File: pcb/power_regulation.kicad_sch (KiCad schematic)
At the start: 40 parts, among them U1 TPS563201, U3 TPS563201, U8 LM1085-5.0, U9 AMS1117-3.3

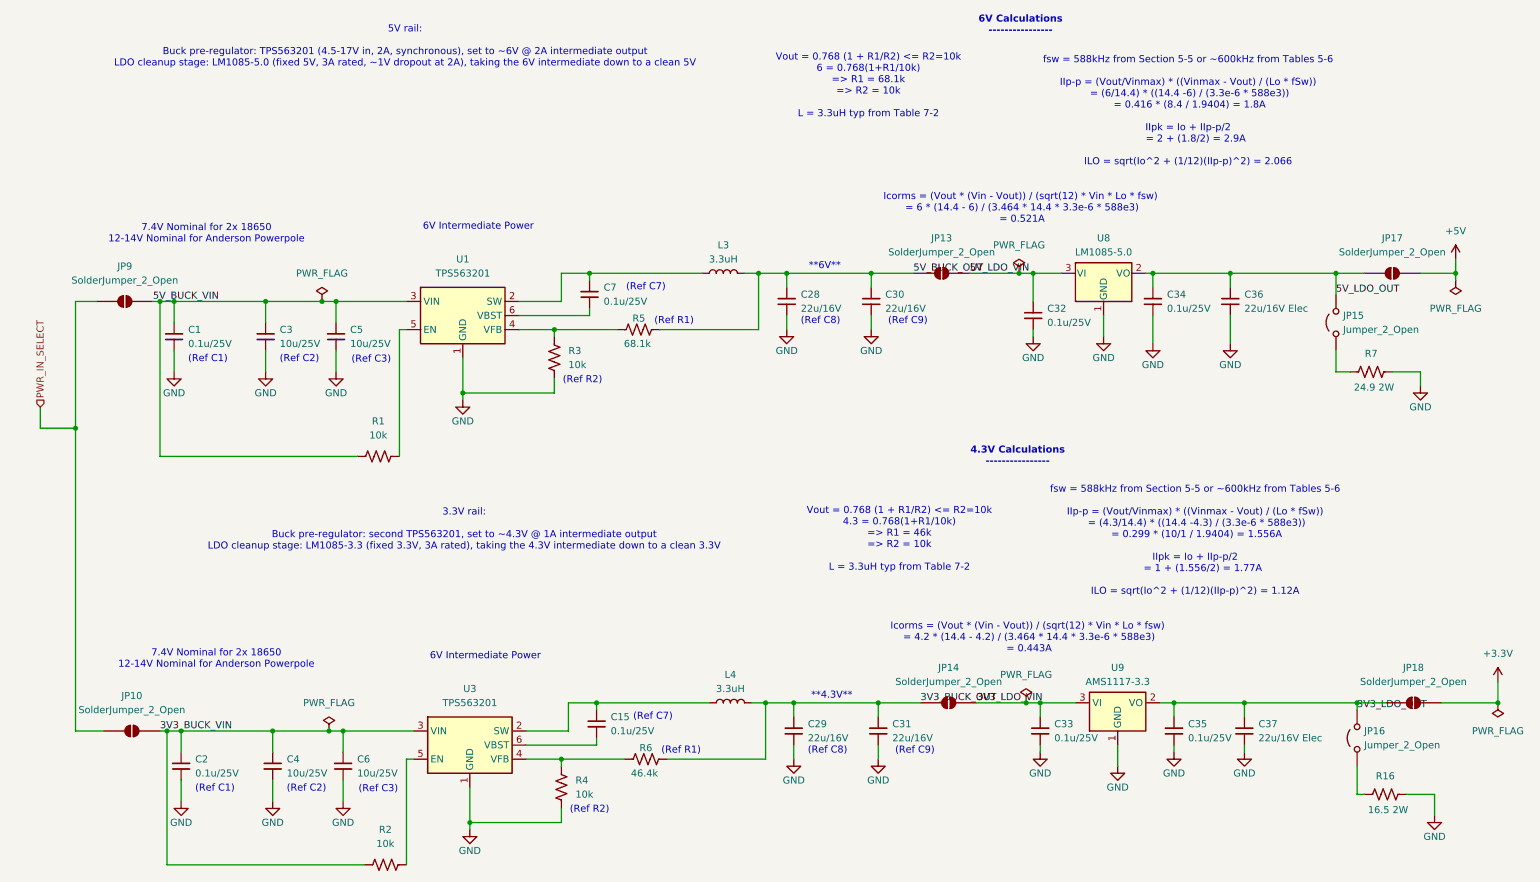
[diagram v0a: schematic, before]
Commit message: Add ESP32-S3 MCU sheet and CH340C USB-UART programming bridge
Restructures the schematic hierarchy: root sheet now hosts three
top-level sheets (Power, mcu-esp32, USB-C Programming UART) instead of
the old flat layout, with the battery/12V ORing-FET merge circuit
moved into its own dedicated Power sheet. Adds the ESP32-S3-WROOM-1
MCU sheet (native USB-C connector stubbed in but not yet wired) and a
CH340C-based USB-UART bridge with auto-reset/bootloader transistor
circuit for programming.

This is a work-in-progress checkpoint — several nets in the new sheets
(MCU decoupling, CH340C power, auto-reset routing, ORing FET gate
drive) still need wiring before ERC will be clean; see prior review
notes for the punch list.

Co-Authored-By: Claude Sonnet 5 <noreply@anthropic.com>
Claude-Session: https://claude.ai/code/session_01LwTJQ9pyVNMigbu4uLMh8c
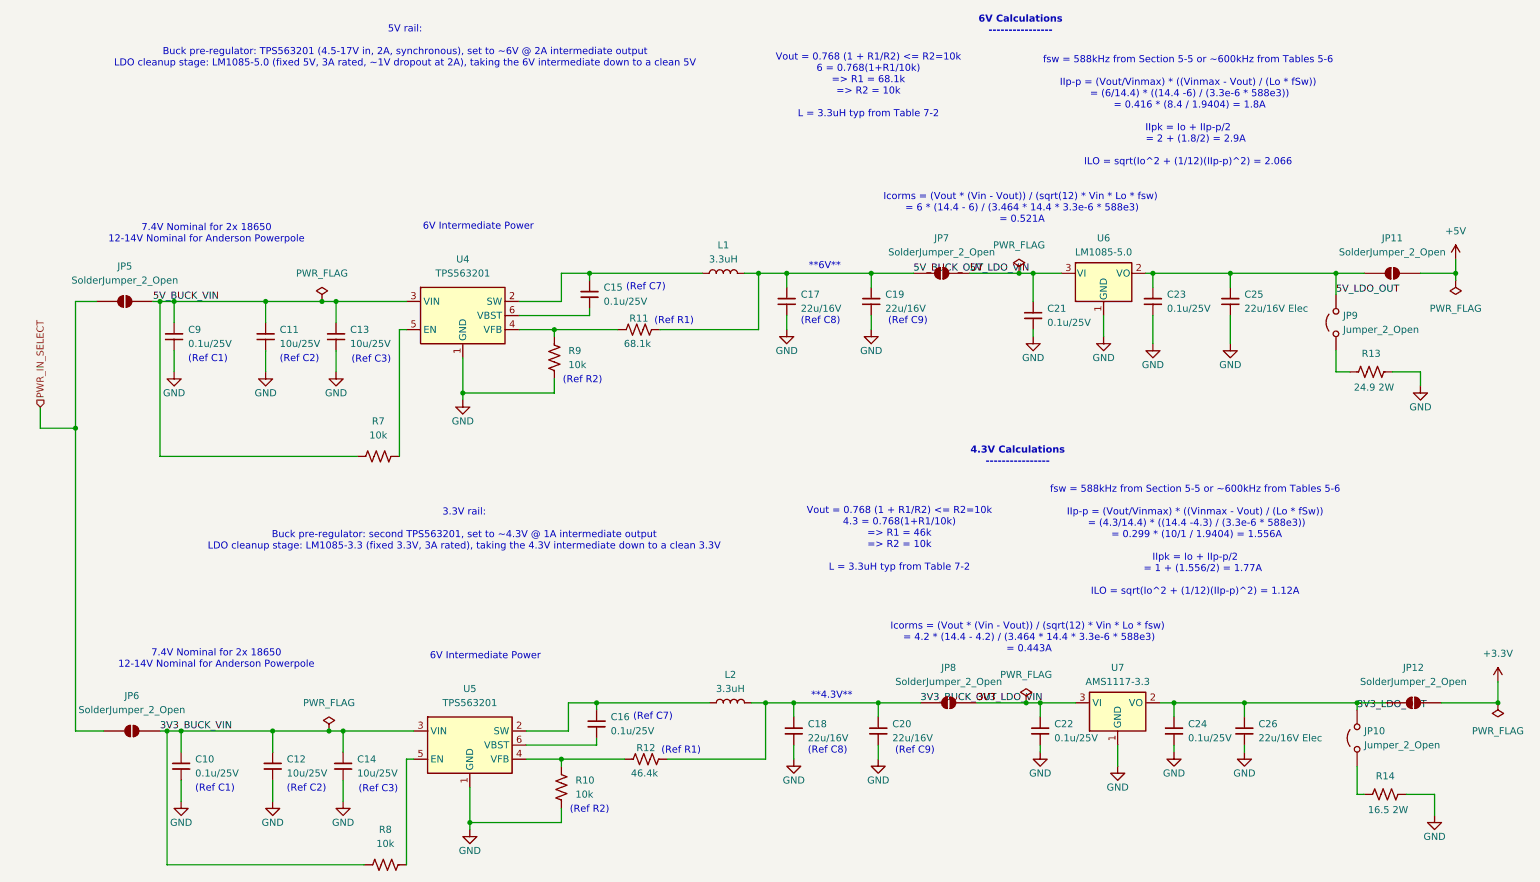
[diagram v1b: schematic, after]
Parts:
- renumbered C2 to C10, C3 to C11, C4 to C12, C5 to C13, C6 to C14, C7 to C15, C15 to C16, C28 to C17, C29 to C18, C30 to C19, C31 to C20, C32 to C21, C33 to C22, C34 to C23, C35 to C24, C36 to C25, C37 to C26, C1 to C9, JP16 to JP10, JP17 to JP11, JP18 to JP12, JP9 to JP5, JP10 to JP6, JP13 to JP7, JP14 to JP8, JP15 to JP9, L3 to L1, L4 to L2, R4 to R10, R5 to R11, R6 to R12, R7 to R13, R16 to R14, R1 to R7, R2 to R8, R3 to R9, U1 to U4, U3 to U5, U8 to U6, U9 to U7
